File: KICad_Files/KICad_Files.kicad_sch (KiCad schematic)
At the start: 42 parts, among them J1 Conn_01x03_MountingPin, J2 Conn_01x03_MountingPin, J3 Conn_01x03_MountingPin, J4 USB_C_Receptacle_USB2.0_14P, J5 Conn_01x06, J6 Conn_01x06, J7 Conn_01x03_Pin, J8 Conn_01x03_Pin, SW1 RESET, SW2 RESET, U1 TPP361061-T6TR, U2 USBLC6-2SC6, U3 ESP32-C3

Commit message: added more descriptions in the schematic
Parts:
- SW1: value RESET -> Boot
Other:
- note added: "5V to 3.3V Buck Converter"
- note added: "Antenna"
- note added: "Boot/Reset Buttons"
- note added: "Bypass Caps"
- note added: "GPIO Pinout"
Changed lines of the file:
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@@
 	)
 	(rectangle
+		(start 109.22 157.48)
+		(end 165.1 194.31)
+		(stroke
+			(width 0)
+			(type dash)
+		)
+		(fill
+			(type none)
+		)
+	)
+	(rectangle
+		(start 227.33 73.66)
+		(end 284.48 113.03)
+		(stroke
+			(width 0)
+			(type dash)
+		)
+		(fill
+			(type none)
+		)
+	)
+	(rectangle
+		(start 194.31 63.5)
+		(end 224.79 87.63)
+		(stroke
+			(width 0)
+			(type dash)
+		)
+		(fill
+			(type none)
+		)
+	)
+	(rectangle
+		(start 214.63 123.19)
+		(end 281.94 157.48)
+		(stroke
+			(width 0)
+			(type dash)
+		)
+		(fill
+			(type none)
+		)
+	)
+	(rectangle
+		(start 19.05 98.298)
+		(end 90.17 186.69)
+		(stroke
+			(width 0)
+			(type dash)
+		)
+		(fill
+			(type none)
+		)
+	)
+	(rectangle
 		(start 20.32 19.05)
 		(end 77.47 62.23)
@@
 		)
 	)
+	(text "Antenna"
+		(exclude_from_sim no)
+		(at 108.966 155.956 0)
+		(effects
+			(font
+				(size 1.27 1.27)
+				(thickness 0.254)
+				(bold yes)
+				(italic yes)
+			)
+			(justify left)
+		)
+	)
+	(text "GPIO Pinout"
+		(exclude_from_sim no)
+		(at 214.63 121.412 0)
+		(effects
+			(font
+				(size 1.27 1.27)
+				(thickness 0.254)
+				(bold yes)
+				(italic yes)
+			)
+			(justify left)
+		)
+	)
+	(text "Bypass Caps"
+		(exclude_from_sim no)
+		(at 194.564 62.23 0)
+		(effects
+			(font
+				(size 1.27 1.27)
+				(thickness 0.254)
+				(bold yes)
+				(italic yes)
+			)
+			(justify left)
+		)
+	)
+	(text "Boot/Reset Buttons"
+		(exclude_from_sim no)
+		(at 227.584 72.644 0)
+		(effects
+			(font
+				(size 1.27 1.27)
+				(thickness 0.254)
+				(bold yes)
+				(italic yes)
+			)
+			(justify left)
+		)
+	)
+	(text "5V to 3.3V Buck Converter"
+		(exclude_from_sim no)
+		(at 19.05 96.52 0)
+		(effects
+			(font
+				(size 1.27 1.27)
+				(thickness 0.254)
+				(bold yes)
+				(italic yes)
+			)
+			(justify left)
+		)
+	)
 	(text "USB-C connector"
 		(exclude_from_sim no)
@@
 			)
 		)
-		(property "Value" "RESET"
+		(property "Value" "Boot"
 			(at 234.696 97.79 90)
 			(effects

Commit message: switched R8/R9 to 10kOhm resistors and properly named switches for Boot/Reset
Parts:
- R8, R9: value 100 -> 10kΩ
- SW1: value Boot -> Reset
- SW2: value RESET -> Boot
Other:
- company: (none) -> Netz39 e.V.
- title: (none) -> ESP32-C3 LED PCB
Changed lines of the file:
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@@
 	(generator_version "8.0")
 	(paper "A4")
+	(title_block
+		(title "ESP32-C3 LED PCB")
+		(date "2025-01-07")
+		(rev "1")
+		(company "Netz39 e.V.")
+	)
 	(junction
 		(at 205.74 69.85)
@@
 	)
 	(junction
+		(at 142.24 54.61)
+		(diameter 0)
+		(color 0 0 0 0)
+	)
+	(junction
 		(at 138.43 91.44)
 		(diameter 0)
@@
 	)
 	(junction
-		(at 142.24 54.61)
-		(diameter 0)
-		(color 0 0 0 0)
-	)
-	(junction
 		(at 213.36 77.47)
 		(diameter 0)
@@
 	(wire
 		(pts
-			(xy 233.68 91.44) (xy 243.84 91.44)
+			(xy 142.24 54.61) (xy 149.86 54.61)
 		)
 		(stroke
@@
 	(wire
 		(pts
-			(xy 252.73 129.54) (xy 250.19 129.54)
+			(xy 233.68 91.44) (xy 243.84 91.44)
 		)
 		(stroke
@@
 	(wire
 		(pts
-			(xy 143.51 173.99) (xy 143.51 168.91)
+			(xy 252.73 129.54) (xy 250.19 129.54)
 		)
 		(stroke
@@
 	(wire
 		(pts
-			(xy 231.14 148.59) (xy 231.14 139.7)
+			(xy 143.51 173.99) (xy 143.51 168.91)
 		)
 		(stroke
@@
 	(wire
 		(pts
-			(xy 273.05 92.71) (xy 273.05 91.44)
+			(xy 231.14 148.59) (xy 231.14 139.7)
 		)
 		(stroke
@@
 	(wire
 		(pts
-			(xy 196.85 104.14) (xy 199.39 104.14)
+			(xy 273.05 92.71) (xy 273.05 91.44)
 		)
 		(stroke
@@
 	(wire
 		(pts
-			(xy 24.13 114.3) (xy 29.21 114.3)
+			(xy 196.85 104.14) (xy 199.39 104.14)
 		)
 		(stroke
@@
 	(wire
 		(pts
-			(xy 135.89 101.6) (xy 151.13 101.6)
+			(xy 24.13 114.3) (xy 29.21 114.3)
 		)
 		(stroke
@@
 	(wire
 		(pts
-			(xy 142.24 54.61) (xy 149.86 54.61)
+			(xy 135.89 101.6) (xy 151.13 101.6)
 		)
 		(stroke
@@
 			)
 		)
-		(property "Value" "100"
+		(property "Value" "10kΩ"
 			(at 140.462 89.916 90)
 			(effects
@@
 	)
 	(symbol
+		(lib_id "power:+5V")
+		(at 142.24 54.61 0)
+		(unit 1)
+		(exclude_from_sim no)
+		(in_bom yes)
+		(on_board yes)
+		(dnp no)
+		(fields_autoplaced yes)
+		(property "Reference" "#PWR014"
+			(at 142.24 58.42 0)
+			(effects
+				(font
+					(size 1.27 1.27)
+				)
+				(hide yes)
+			)
+		)
+		(property "Value" "+5V"
+			(at 142.24 49.53 0)
+			(effects
+				(font
+					(size 1.27 1.27)
+				)
+			)
+		)
+		(property "Footprint" ""
+			(at 142.24 54.61 0)
+			(effects
+				(font
+					(size 1.27 1.27)
+				)
+				(hide yes)
+			)
+		)
+		(property "Datasheet" ""
+			(at 142.24 54.61 0)
+			(effects
+				(font
+					(size 1.27 1.27)
+				)
+				(hide yes)
+			)
+		)
+		(property "Description" "Power symbol creates a global label with name \"+5V\""
+			(at 142.24 54.61 0)
+			(effects
+				(font
+					(size 1.27 1.27)
+				)
+				(hide yes)
+			)
+		)
+		(pin "1"
+		)
+		(instances
+			(project "KICad_Files"
+				(path "/34061aa1-1595-4a0a-9524-9b9b15681d54"
+					(reference "#PWR014")
+					(unit 1)
+				)
+			)
+		)
+	)
+	(symbol
 		(lib_id "Connector_Generic:Conn_01x03")
 		(at 49.53 50.8 0)
@@
 	)
 	(symbol
-		(lib_id "power:+5V")
-		(at 142.24 54.61 0)
-		(unit 1)
-		(exclude_from_sim no)
-		(in_bom yes)
-		(on_board yes)
-		(dnp no)
-		(fields_autoplaced yes)
-		(property "Reference" "#PWR014"
-			(at 142.24 58.42 0)
-			(effects
-				(font
-					(size 1.27 1.27)
-				)
-				(hide yes)
-			)
-		)
-		(property "Value" "+5V"
-			(at 142.24 49.53 0)
-			(effects
-				(font
-					(size 1.27 1.27)
-				)
-			)
-		)
-		(property "Footprint" ""
-			(at 142.24 54.61 0)
-			(effects
-				(font
-					(size 1.27 1.27)
-				)
-				(hide yes)
-			)
-		)
-		(property "Datasheet" ""
-			(at 142.24 54.61 0)
-			(effects
-				(font
-					(size 1.27 1.27)
-				)
-				(hide yes)
-			)
-		)
-		(property "Description" "Power symbol creates a global label with name \"+5V\""
-			(at 142.24 54.61 0)
-			(effects
-				(font
-					(size 1.27 1.27)
-				)
-				(hide yes)
-			)
-		)
-		(pin "1"
-		)
-		(instances
-			(project "KICad_Files"
-				(path "/34061aa1-1595-4a0a-9524-9b9b15681d54"
-					(reference "#PWR014")
-					(unit 1)
-				)
-			)
-		)
-	)
-	(symbol
 		(lib_id "Connector:Conn_01x03_Pin")
 		(at 276.86 130.81 180)
@@
 			)
 		)
-		(property "Value" "Boot"
+		(property "Value" "Reset"
 			(at 234.696 97.79 90)
 			(effects
@@
 			)
 		)
-		(property "Value" "100"
+		(property "Value" "10kΩ"
 			(at 140.462 95.25 90)
 			(effects
@@
 			)
 		)
-		(property "Value" "RESET"
+		(property "Value" "Boot"
 			(at 263.906 97.79 90)
 			(effects

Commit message: rework of the PCB Layout
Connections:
- net +3.3V: now also L1.1; no longer L1.2
- net GPIO 13: now also J7.2 (Pin_2); no longer J7.1 (Pin_1)
- net GPIO 14: now also J7.1 (Pin_1); no longer J7.2 (Pin_2)
- net at R1.2, U1.6 (SW): now also L1.2; no longer L1.1
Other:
- moved on the sheet: L1
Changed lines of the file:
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@@
 	)
 	(label "GPIO 13"
-		(at 269.24 133.35 180)
+		(at 269.24 130.81 180)
 		(fields_autoplaced yes)
 		(effects
@@
 	)
 	(label "GPIO 14"
-		(at 269.24 130.81 180)
+		(at 269.24 133.35 180)
 		(fields_autoplaced yes)
 		(effects
@@
 	(symbol
 		(lib_id "Device:L")
-		(at 35.56 153.67 90)
-		(unit 1)
-		(exclude_from_sim no)
+		(at 35.56 153.67 270)
+		(mirror x)
+		(unit 1)
+		(exclude_from_sim no)

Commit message: fixed placement of silkscreen and improoved flow of the GND-plane
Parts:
- R2: value 10 kΩ -> 15kΩ
- R3: value 220kΩ -> 68kΩ
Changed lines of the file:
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@@
 			)
 		)
-		(property "Value" "10 kΩ"
+		(property "Value" "15kΩ"
 			(at 48.006 160.02 90)
 			(effects
@@
 			)
 		)
-		(property "Value" "220kΩ"
+		(property "Value" "68kΩ"
 			(at 48.006 176.022 90)
 			(effects

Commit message: added the correct values to the voltage divider
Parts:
- R2: value 15kΩ -> 68kΩ
- R3: value 68kΩ -> 15kΩ
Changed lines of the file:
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@@
 			)
 		)
-		(property "Value" "15kΩ"
+		(property "Value" "68kΩ"
 			(at 48.006 160.02 90)
 			(effects
@@
 			)
 		)
-		(property "Value" "68kΩ"
+		(property "Value" "15kΩ"
 			(at 48.006 176.022 90)
 			(effects

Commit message: added multiple components for proper operation of the ESP added 40 mHz crystal added a connector for UART Changed LED placement to GPIO8 for use as Debug LED
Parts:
- removed D1: LED, LED_SMD:LED_0805_2012Metric_Pad1.15x1.40mm_HandSolder, symbol Device:LED
- removed R4: 560Ω, Resistor_SMD:R_0603_1608Metric_Pad0.98x0.95mm_HandSolder, symbol Device:R
- added 26pF1: C, symbol Device:C
- added C10: 26pF, symbol Device:C
- added D3: LED, LED_SMD:LED_0805_2012Metric_Pad1.15x1.40mm_HandSolder, symbol Device:LED
- added J9: Conn_01x03, symbol Connector_Generic:Conn_01x03
- added R12: 560Ω, Resistor_SMD:R_0603_1608Metric_Pad0.98x0.95mm_HandSolder, symbol Device:R
- added Y1: 40.0MHz, Crystal:Crystal_SMD_3225-4Pin_3.2x2.5mm, symbol Device:Crystal_GND24
- renumbered C8 to C1, C4 to C11, C5 to C12, C6 to C13, C7 to C14, C9 to C2, C10 to C3, C11 to C4, C12 to C5, C13 to C6, C1 to C7, C2 to C8, C3 to C9, J4 to J2, J2 to J3, J3 to J4, J7 to J5, J5 to J6, J6 to J7, R5 to R10, R3 to R11, R6 to R2, R7 to R3, R10 to R4, R11 to R5, R8 to R6, R9 to R7, R1 to R8, R2 to R9, U3 to U1, U1 to U3
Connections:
- net GND is gone; now on net +5V: C1.2, C11.1, C12.1, C13.2, C14.2, C2.2, C3.2, C4.2, C5.2, C6.2, C8.1, C9.1, D2.1 (K), J1.3 (Pin_3), J2.A1 (GND), J2.A12 (GND), J2.B1 (GND), J2.B12 (GND), J2.S1 (SHIELD), J3.3 (Pin_3), J4.3 (Pin_3), J6.6 (Pin_6), J7.6 (Pin_6), R11.1, R2.1, R3.1, SW1.1, SW2.1, U1.33 (GND), U2.2 (GND), U3.2 (GND)
- net +3.3V: no longer R6.1
- net +5V: now also R6.1, 26pF1.2, C10.2, D3.1 (K), J9.3 (Pin_3), Y1.2, Y1.4
- net CHIP_EN: now reaches C5.1, R4.2, SW1.2, U1.7 (CHIP_EN)
- net at R7.2, U1.14 (GPIO8): now also R12.2
- net U0RXD: now reaches U1.27 (U0RXD)
- net U0RXD: now also J9.2 (Pin_2)
- net U0TXD: now reaches U1.28 (U0TXD)
- net U0TXD: now also J9.1 (Pin_1)
- net XTAL_N: now reaches U1.29 (XTAL_N)
- net XTAL_N: now also 26pF1.1, Y1.3
- net XTAL_P: now reaches U1.30 (XTAL_P)
- net XTAL_P: now also C10.1, Y1.1
- new net: D3.2 (A), R12.1
- no-connect marks 8 -> 4
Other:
- note added: "Boot(y) /Reset Buttons"
- note added: "Crystal"
- note added: "Debug LED"
- note added: "ESP32-C3"
- note removed: "Boot/Reset Buttons"
- moved on the sheet: AE1, C1, C11, C12, C13, C14, C2, C3, C4, C5, C6, C7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

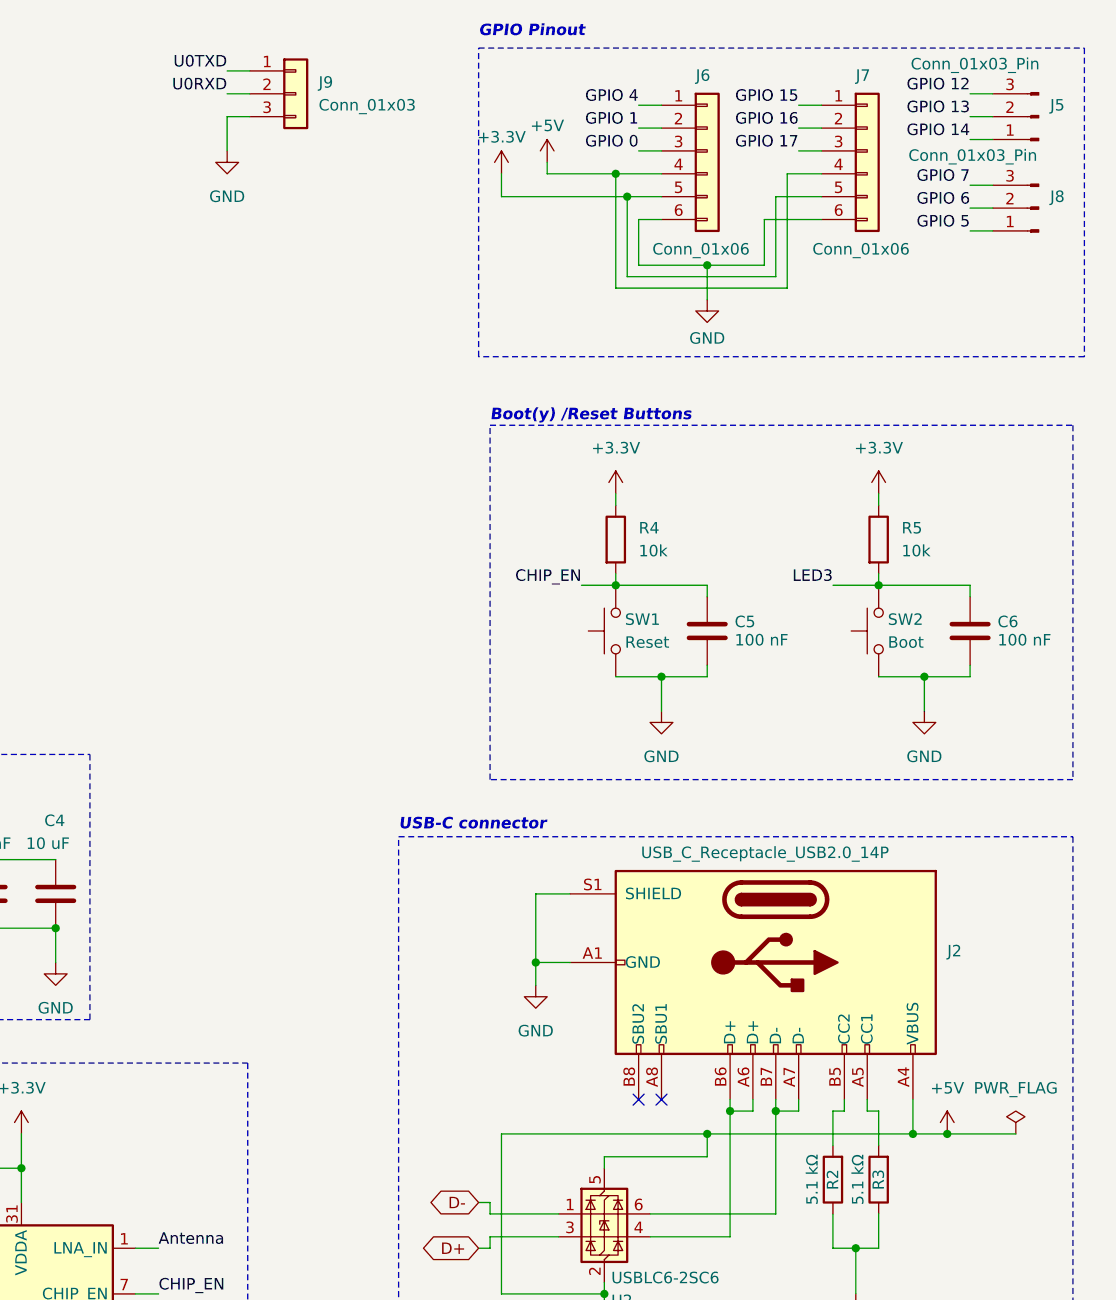
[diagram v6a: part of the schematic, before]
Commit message: added footprints to the added parts
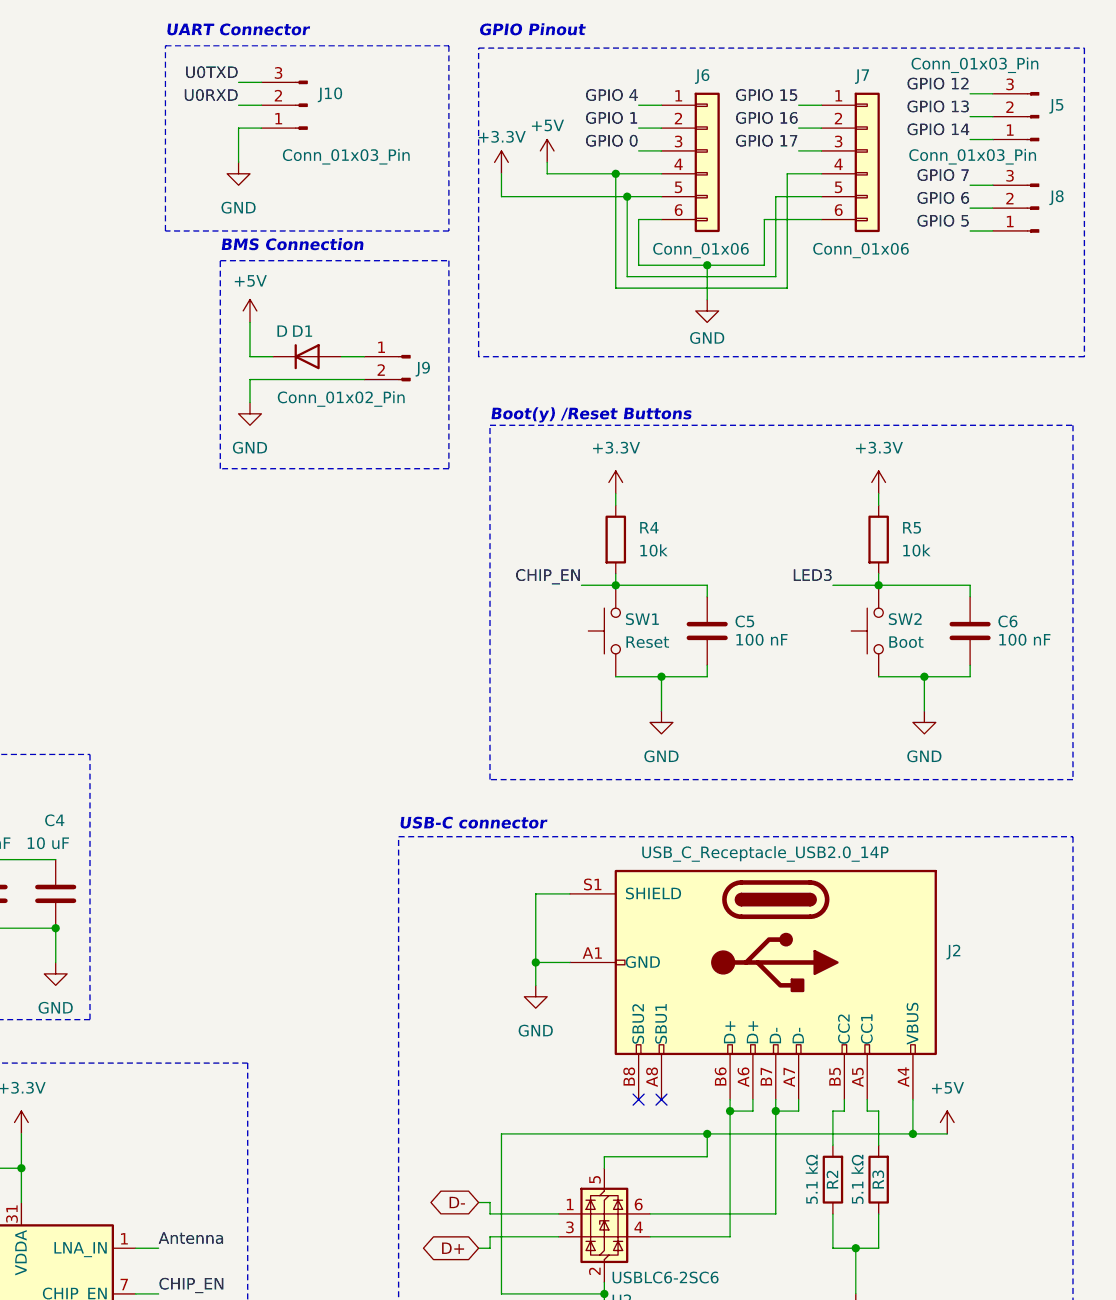
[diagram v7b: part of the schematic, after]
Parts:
- removed J9: Conn_01x03, symbol Connector_Generic:Conn_01x03
- added D1: D, Diode_SMD:D_0603_1608Metric_Pad1.05x0.95mm_HandSolder, symbol Device:D
- added J10: Conn_01x03_Pin, Connector_PinHeader_2.00mm:PinHeader_1x03_P2.00mm_Vertical, symbol Connector:Conn_01x03_Pin
- added J9: Conn_01x02_Pin, Connector_PinHeader_1.00mm:PinHeader_1x02_P1.00mm_Vertical, symbol Connector:Conn_01x02_Pin
- 26pF1, C10: footprint (none) -> Capacitor_SMD:C_0603_1608Metric_Pad1.08x0.95mm_HandSolder
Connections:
- net +5V: now also D1.1 (K), J10.1 (Pin_1), J9.2 (Pin_2)
- net U0RXD: now also J10.2 (Pin_2)
- net U0TXD: now also J10.3 (Pin_3)
- new net: D1.2 (A), J9.1 (Pin_1)
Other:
- note added: "BMS Connection"
- note added: "UART Connector"
